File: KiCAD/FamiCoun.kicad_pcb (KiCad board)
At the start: 2 copper layers, 143.3 x 18.9 mm, 6 parts, among them P1 DA15, P1-NES1 NES_7P_PORT, P1-NES2 NES_7P_PORT, P1-SNES1 SNES_7P_PORT, P1-SNES2 SNES_7P_PORT

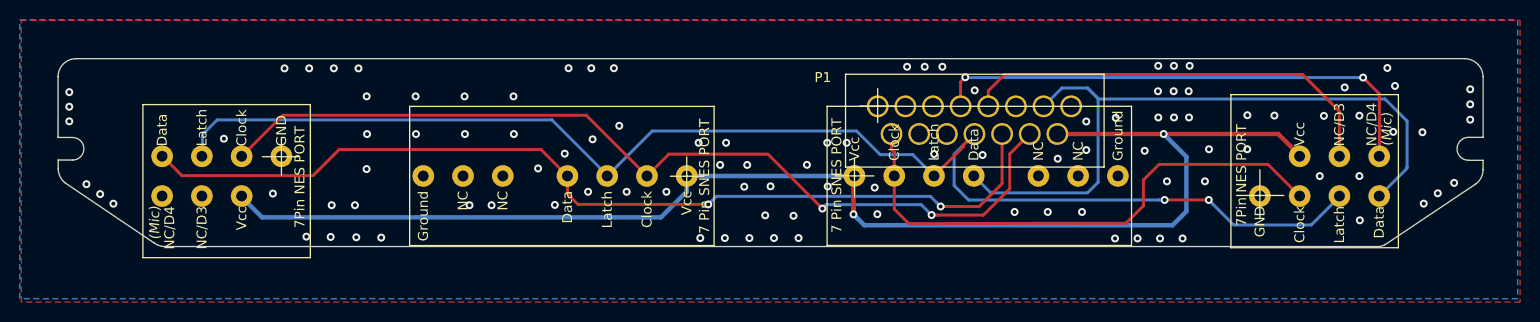
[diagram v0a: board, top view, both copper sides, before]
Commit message: Fix dimensions
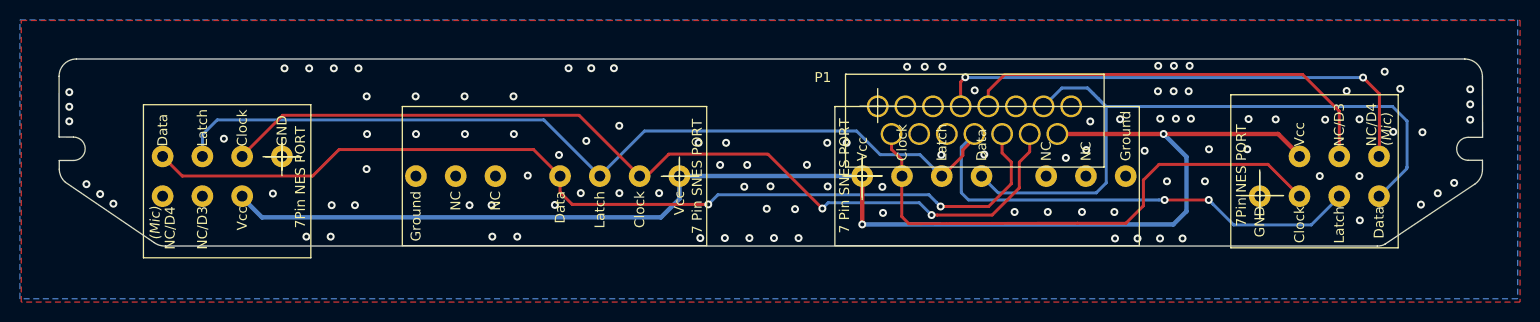
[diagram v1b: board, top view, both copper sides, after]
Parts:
- removed the G*** at (159.4, 96.5)
- added G***: LOGO, FamiCoun:PCB_outline_new, F.Cu at (159.4, 96.5)
- moved P1-SNES2 0.78 mm to (168.6, 98.9)
- moved P1-SNES1 0.74 mm to (150.3, 98.9)
- moved P1-NES1 0.05 mm to (104.3, 98.9)
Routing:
- net Net-(P1-NES1-Pad4): track 96.1 -> 98.6 mm
- net Net-(P1-NES2-Pad4): track 71.0 -> 72.2 mm
- net Net-(P1-NES1-Pad2): track 92.7 -> 93.4 mm
- net GND: vias 108 -> 109
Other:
- board size 143.3 x 18.9 mm -> 143.2 x 18.8 mm
